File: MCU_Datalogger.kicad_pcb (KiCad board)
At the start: 2 copper layers, 50.5 x 40.2 mm, 29 parts, among them J1 Conn_01x02_Pin, J2 Conn_01x04_Pin, J3 Conn_01x04_Pin, J4 Conn_01x09_Pin, J5 Conn_02x03_Odd_Even, U1 24LC1025, U2 24LC1025, U3 DS1337S_, U4 ATMEGA328P-AU, Y1 32.768kHz, Y2 16MHz

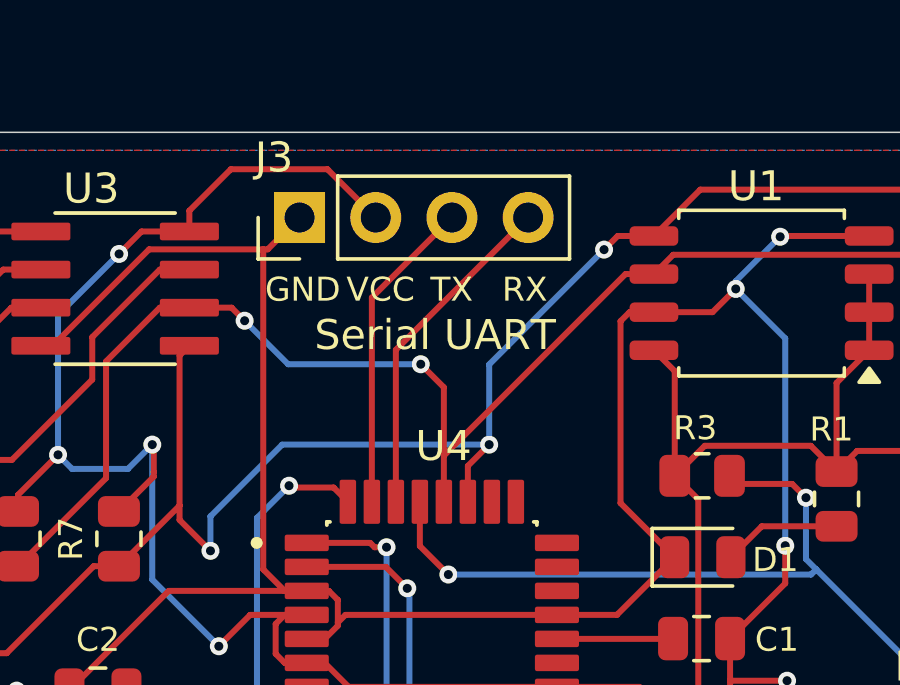
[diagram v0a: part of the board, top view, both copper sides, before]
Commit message: Fixed RX TX misconnections
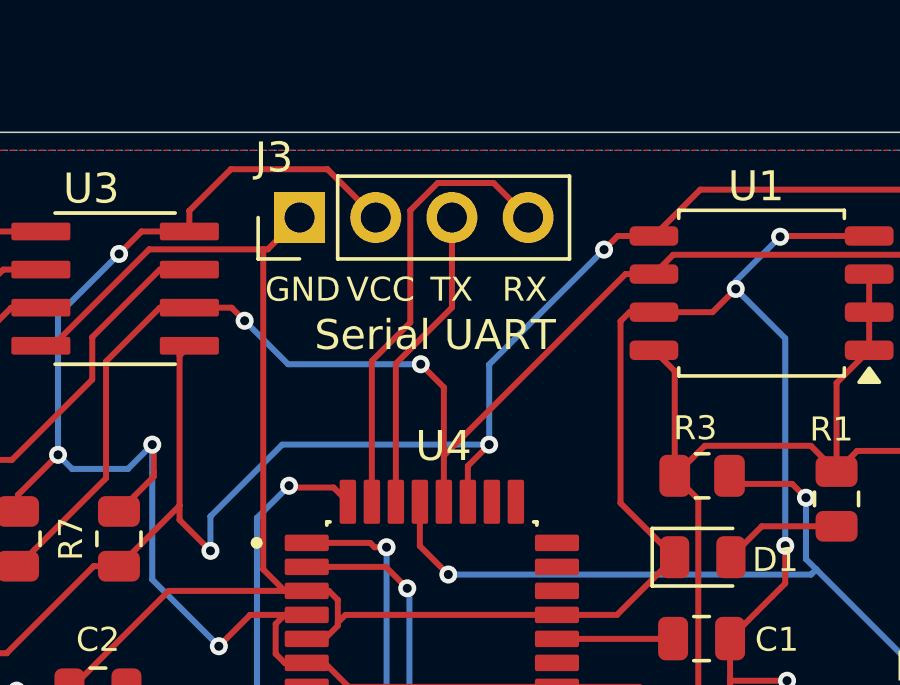
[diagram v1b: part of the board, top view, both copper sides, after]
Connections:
- J3 pad 3: /TX -> /RX
- J3 pad 4: /RX -> /TX
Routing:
- net /TX: track 10.6 -> 15.0 mm
- net /RX: track 11.3 -> 10.2 mm
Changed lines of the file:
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@@
 			(layers "*.Cu" "*.Mask")
 			(remove_unused_layers no)
-			(net 10 "/TX")
+			(net 11 "/RX")
 			(pinfunction "Pin_3")
 			(pintype "passive")
@@
 			(layers "*.Cu" "*.Mask")
 			(remove_unused_layers no)
-			(net 11 "/RX")
+			(net 10 "/TX")
 			(pinfunction "Pin_4")
 			(pintype "passive")
@@
 		(sheetname "/Connectors/")
 		(sheetfile "untitled.kicad_sch")
-		(attr through_hole exclude_from_bom)
+		(attr through_hole)
 		(fp_line
 			(start -1.38 -1.38)
@@
 	)
 	(segment
-		(start 127.43 105.56)
-		(end 130.1 102.89)
+		(start 127.43 107.67)
+		(end 127.43 112.3652)
 		(width 0.2)
 		(layer "F.Cu")
@@
 	)
 	(segment
-		(start 127.43 112.3652)
-		(end 127.43 105.56)
+		(start 132.64 102.89)
+		(end 131.489 101.739)
 		(width 0.2)
 		(layer "F.Cu")
@@
 	)
 	(segment
-		(start 128.23 107.3)
-		(end 132.64 102.89)
+		(start 129.62324 101.739)
+		(end 128.711 102.65124)
 		(width 0.2)
 		(layer "F.Cu")
-		(net 11)
+		(net 10)
+	)
+	(segment
+		(start 128.711 106.389)
+		(end 127.43 107.67)
+		(width 0.2)
+		(layer "F.Cu")
+		(net 10)
+	)
+	(segment
+		(start 131.489 101.739)
+		(end 129.62324 101.739)
+		(width 0.2)
+		(layer "F.Cu")
+		(net 10)
+	)
+	(segment
+		(start 128.711 102.65124)
+		(end 128.711 106.389)
+		(width 0.2)
+		(layer "F.Cu")
+		(net 10)
 	)
 	(segment
 		(start 128.23 112.3652)
-		(end 128.23 107.3)
+		(end 128.23 107.760057)
+		(width 0.2)
+		(layer "F.Cu")
+		(net 11)
+	)
+	(segment
+		(start 130.1 105.890057)
+		(end 130.1 102.89)
+		(width 0.2)
+		(layer "F.Cu")
+		(net 11)
+	)
+	(segment
+		(start 128.23 107.760057)
+		(end 130.1 105.890057)
 		(width 0.2)
 		(layer "F.Cu")

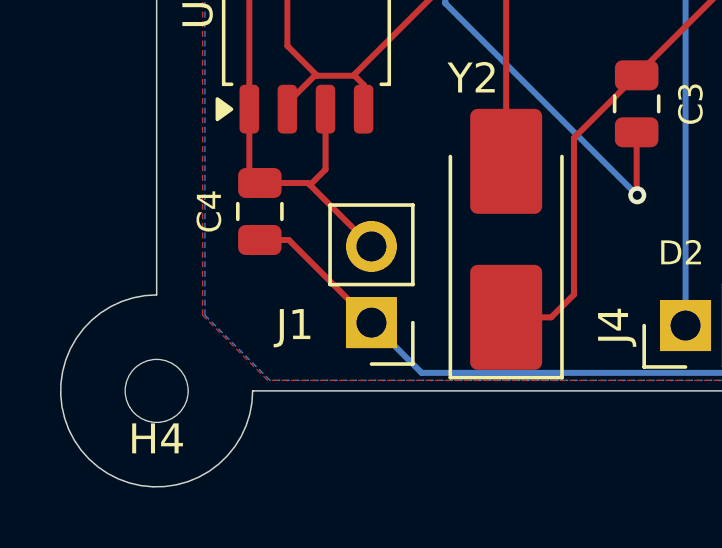
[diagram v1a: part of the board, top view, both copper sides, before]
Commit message: Edited BAT footprint placement and silkscreen info
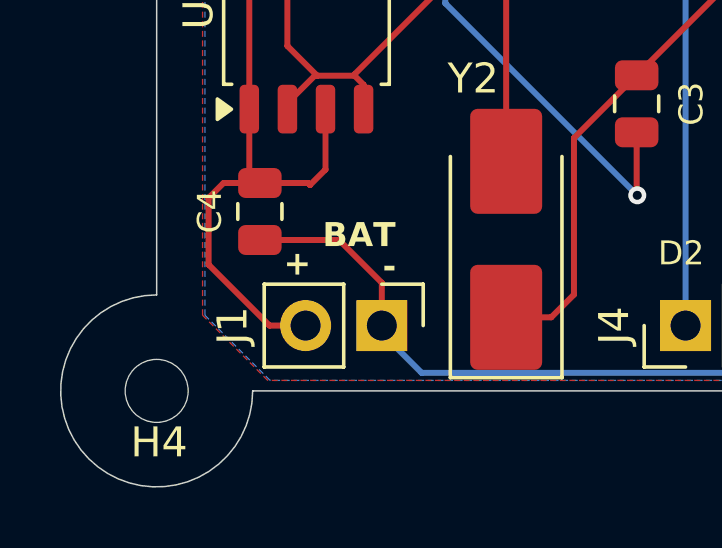
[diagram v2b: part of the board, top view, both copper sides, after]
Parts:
- moved J1 0.36 mm to (113.5, 131.8), turned to -90 degrees
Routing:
- net VCC: track 138.6 -> 143.9 mm
- net GND: track 181.0 -> 182.2 mm
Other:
- board text added: "+"
- board text added: "-"
- board text added: "BAT"
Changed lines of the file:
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@@
 	(footprint "Connector_PinHeader_2.54mm:PinHeader_1x02_P2.54mm_Vertical"
 		(layer "F.Cu")
-		(at 113.13 131.705 180)
+		(at 113.475 131.8025 -90)
 		(descr "Through hole straight pin header, 1x02, 2.54mm pitch, single row")
 		(tags "Through hole pin header THT 1x02 2.54mm single row")
 		(property "Reference" "J1"
-			(at 2.55 -0.085 0)
+			(at 0 4.975 90)
 			(layer "F.SilkS")
 			(effects
@@
 		)
 		(property "Value" "Conn_01x02_Pin"
-			(at 0 4.92 0)
+			(at 0 4.92 90)
 			(layer "F.Fab")
 			(effects
@@
 		)
 		(property "Datasheet" "~"
-			(at 0 0 0)
+			(at 0 0 90)
 			(layer "F.Fab")
 			(hide yes)
@@
 		)
 		(property "Description" "Generic connector, single row, 01x02, script generated"
-			(at 0 0 0)
+			(at 0 0 90)
 			(layer "F.Fab")
 			(hide yes)
@@
 		(attr through_hole)
 		(fp_line
-			(start 1.38 1.27)
+			(start -1.38 3.92)
 			(end 1.38 3.92)
 			(stroke
@@
 		)
 		(fp_line
-			(start -1.38 3.92)
-			(end 1.38 3.92)
+			(start -1.38 1.27)
+			(end -1.38 3.92)
 			(stroke
 				(width 0.12)
@@
 		)
 		(fp_line
-			(start -1.38 1.27)
-			(end -1.38 3.92)
+			(start 1.38 1.27)
+			(end 1.38 3.92)
 			(stroke
 				(width 0.12)
@@
 		)
 		(fp_line
-			(start 1.27 3.81)
-			(end -1.27 3.81)
+			(start -1.27 3.81)
+			(end -1.27 -0.635)
 			(stroke
 				(width 0.1)
@@
 		)
 		(fp_line
-			(start 1.27 -1.27)
-			(end 1.27 3.81)
+			(start 1.27 3.81)
+			(end -1.27 3.81)
 			(stroke
 				(width 0.1)
@@
 		)
 		(fp_line
-			(start -0.635 -1.27)
-			(end 1.27 -1.27)
+			(start -1.27 -0.635)
+			(end -0.635 -1.27)
 			(stroke
 				(width 0.1)
@@
 		)
 		(fp_line
-			(start -1.27 3.81)
-			(end -1.27 -0.635)
+			(start -0.635 -1.27)
+			(end 1.27 -1.27)
 			(stroke
 				(width 0.1)
@@
 		)
 		(fp_line
-			(start -1.27 -0.635)
-			(end -0.635 -1.27)
+			(start 1.27 -1.27)
+			(end 1.27 3.81)
 			(stroke
 				(width 0.1)
@@
 		)
 		(fp_text user "${REFERENCE}"
-			(at 0 1.27 90)
+			(at 0 1.27 0)
 			(layer "F.Fab")
 			(effects
@@
 		)
 		(pad "1" thru_hole rect
-			(at 0 0 180)
+			(at 0 0 270)
 			(size 1.7 1.7)
 			(drill 1)
@@
 		)
 		(pad "2" thru_hole circle
-			(at 0 2.54 180)
+			(at 0 2.54 270)
 			(size 1.7 1.7)
 			(drill 1)
@@
 		(tags "mountinghole")
 		(property "Reference" "H4"
-			(at 0 1.62 0)
+			(at 0.08 1.72 0)
 			(layer "F.SilkS")
 			(effects
@@
 		)
 	)
+	(gr_text "-"
+		(at 113.5 130.3 0)
+		(layer "F.SilkS")
+		(effects
+			(font
+				(size 0.8 0.8)
+				(thickness 0.16)
+				(bold yes)
+			)
+			(justify left bottom)
+		)
+	)
 	(gr_text "VCC\n"
 		(at 126.58 105.76 0)
@@
 		)
 	)
+	(gr_text "+"
+		(at 110.2 130.2 0)
+		(layer "F.SilkS")
+		(effects
+			(font
+				(size 0.8 0.8)
+				(thickness 0.16)
+				(bold yes)
+			)
+			(justify left bottom)
+		)
+	)
 	(gr_text "GND"
 		(at 139.815834 129.86 0)
@@
 		)
 	)
+	(gr_text "BAT"
+		(at 111.5 129.25 0)
+		(layer "F.SilkS")
+		(effects
+			(font
+				(size 0.8 0.8)
+				(thickness 0.16)
+				(bold yes)
+			)
+			(justify left bottom)
+		)
+	)
 	(gr_text "D2"
 		(at 122.68 129.86 0)
@@
 	)
 	(segment
-		(start 110.375 128.95)
-		(end 109.41 128.95)
-		(width 0.2)
-		(layer "F.Cu")
-		(net 1)
-	)
-	(segment
 		(start 141.21 115.086)
 		(end 141.21 113.83)
@@
 	)
 	(segment
-		(start 112.566999 123.426401)
-		(end 112.566999 123.474)
+		(start 112.05 128.95)
+		(end 109.41 128.95)
 		(width 0.2)
 		(layer "F.Cu")
@@
 	)
 	(segment
-		(start 138.785 106.045)
-		(end 136.8325 106.045)
+		(start 112.566999 123.426401)
+		(end 112.566999 123.474)
 		(width 0.2)
 		(layer "F.Cu")
@@
 	)
 	(segment
-		(start 113.13 131.705)
-		(end 110.375 128.95)
+		(start 138.785 106.045)
+		(end 136.8325 106.045)
 		(width 0.2)
 		(layer "F.Cu")
@@
 	)
 	(segment
+		(start 113.475 130.375)
+		(end 112.05 128.95)
+		(width 0.2)
+		(layer "F.Cu")
+		(net 1)
+	)
+	(segment
 		(start 139.3475 125.96)
 		(end 142.24 123.0675)
@@
 	)
 	(segment
+		(start 113.475 131.8025)
+		(end 113.475 130.375)
+		(width 0.2)
+		(layer "F.Cu")
+		(net 1)
+	)
+	(segment
 		(start 126.5508 116.1352)
 		(end 133.6 116.1352)
@@
 	)
 	(segment
-		(start 139.56 105.011)
-		(end 139.56 105.27)
+		(start 141.04 103.531)
+		(end 139.56 105.011)
 		(width 0.2)
 		(layer "B.Cu")
@@
 	)
 	(segment
-		(start 141.04 103.531)
-		(end 139.56 105.011)
+		(start 115.59 118.66)
+		(end 115.59 121.06)
 		(width 0.2)
 		(layer "B.Cu")
@@
 	)
 	(segment
-		(start 115.59 118.66)
-		(end 115.59 121.06)
+		(start 139.56 105.011)
+		(end 139.56 105.27)
 		(width 0.2)
 		(layer "B.Cu")
@@
 	)
 	(segment
+		(start 110.935 131.8025)
+		(end 109.732919 131.8025)
+		(width 0.2)
+		(layer "F.Cu")
+		(net 5)
+	)
+	(segment
 		(start 120.16 110.51)
 		(end 120.11 110.46)
@@
 	)
 	(segment
+		(start 109.732919 131.8025)
+		(end 107.7 129.769581)
+		(width 0.2)
+		(layer "F.Cu")
+		(net 5)
+	)
+	(segment
 		(start 121.347 102.663)
 		(end 121.347 103.355)
@@
 	)
 	(segment
+		(start 108.2 127.05)
+		(end 109.41 127.05)
+		(width 0.2)
+		(layer "F.Cu")
+		(net 5)
+	)
+	(segment
 		(start 111.598 126.602)
 		(end 111.0825 127.1175)
@@
 	)
 	(segment
-		(start 113.13 129.165)
-		(end 111.0825 127.1175)
-		(width 0.2)
-		(layer "F.Cu")
-		(net 5)
-	)
-	(segment
 		(start 127.56 102.89)
 		(end 125.95 101.28)
@@
 	)
 	(segment
+		(start 107.7 127.55)
+		(end 108.2 127.05)
+		(width 0.2)
+		(layer "F.Cu")
+		(net 5)
+	)
+	(segment
 		(start 108.908 114.5125)
 		(end 112.272 114.5125)
@@
 		(width 0.2)
 		(layer "F.Cu")
+		(net 5)
+	)
+	(segment
+		(start 107.7 129.769581)
+		(end 107.7 127.55)
+		(width 0.2)
+		(layer "F.Cu")

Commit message: 4 Layer board setup
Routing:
- net GND: track 182.2 -> 0.00 mm, vias 7 -> 0
- net VCC: track 143.9 -> 0.00 mm, vias 4 -> 0
- net /SDA: track 59.4 -> 0.00 mm, vias 3 -> 0
- net /SCL: track 51.9 -> 0.00 mm, vias 2 -> 0
- net /RESET: track 28.6 -> 0.00 mm, vias 2 -> 0
- net /MOSI: track 22.7 -> 0.00 mm, vias 1 -> 0
- net /D2: track 22.6 -> 0.00 mm, vias 1 -> 0
- net /D3: track 21.4 -> 0.00 mm, vias 1 -> 0
- net /D4: track 20.2 -> 0.00 mm, vias 1 -> 0
- net /SCK: track 18.2 -> 0.00 mm
- net /MISO: track 16.8 -> 0.00 mm, vias 1 -> 0
- net Net-(U4-PB7): track 16.2 -> 0.00 mm
- net /D8: track 15.2 -> 0.00 mm
- net /TX: track 15.0 -> 0.00 mm
- net /D7: track 14.4 -> 0.00 mm
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- removed copper zone on B.Cu, net GND
- removed copper zone on F.Cu, net VCC
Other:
- copper layers 2 -> 4

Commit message: Completed 4 Layer PCB Layout
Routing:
- net GND: track 0.00 -> 156.4 mm, vias 0 -> 5
- net VCC: track 0.00 -> 100.0 mm, vias 0 -> 3
- net /SCL: track 0.00 -> 63.1 mm, vias 0 -> 2
- net /SDA: track 0.00 -> 62.1 mm, vias 0 -> 2
- net /RESET: track 0.00 -> 38.6 mm, vias 0 -> 1
- net /MOSI: track 0.00 -> 23.1 mm
- net /D2: track 0.00 -> 23.0 mm, vias 0 -> 1
- net /D3: track 0.00 -> 20.8 mm, vias 0 -> 1
- net /D4: track 0.00 -> 19.6 mm, vias 0 -> 1
- net /MISO: track 0.00 -> 19.2 mm
- net /SCK: track 0.00 -> 17.5 mm
- net Net-(U4-PB7): track 0.00 -> 16.1 mm
- net /TX: track 0.00 -> 15.9 mm
- net /D8: track 0.00 -> 15.2 mm
- net /D7: track 0.00 -> 14.4 mm
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- added copper zone on B.Cu, net GND
- added copper zone on In2.Cu, net VCC

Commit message: Edited Copper fills
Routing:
- added copper zone on B.Cu, net /MISO
- removed copper zone on B.Cu, net GND
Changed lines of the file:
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@@
 	)
 	(zone
-		(net 1)
-		(net_name "GND")
+		(net 20)
+		(net_name "/MISO")
 		(layer "B.Cu")
 		(hatch edge 0.5)
@@
 		(filled_areas_thickness no)
 		(fill yes
+			(mode hatch)
 			(thermal_gap 0.5)
 			(thermal_bridge_width 0.5)
+			(hatch_thickness 1)
+			(hatch_gap 1.5)
+			(hatch_orientation 0)
+			(hatch_border_algorithm hatch_thickness)
+			(hatch_min_hole_area 0.3)
 		)
 		(polygon
@@
 		(filled_areas_thickness no)
 		(fill yes
+			(mode hatch)
 			(thermal_gap 0.5)
 			(thermal_bridge_width 0.5)
+			(hatch_thickness 1)
+			(hatch_gap 1.5)
+			(hatch_orientation 0)
+			(hatch_border_algorithm hatch_thickness)
+			(hatch_min_hole_area 0.3)
 		)
 		(polygon

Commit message: Added README
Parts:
- moved C4 27.6 mm to (119.0, 102.1), turned to 180 degrees
- moved U3 2.30 mm to (117.6, 107.2)
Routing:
- net VCC: track 100.0 -> 96.2 mm, vias 3 -> 5
- net GND: track 156.4 -> 152.9 mm
- net /SDA: track 62.1 -> 59.8 mm
- net Net-(U3-X2): track 8.45 -> 6.37 mm
- net Net-(U3-SQW/~INT): track 12.4 -> 10.3 mm
- net Net-(U3-~{INTA}): track 11.5 -> 9.43 mm
- net Net-(U3-X1): track 6.82 -> 5.37 mm
- added copper zone on B.Cu, net GND
- removed copper zone on B.Cu, net /MISO
